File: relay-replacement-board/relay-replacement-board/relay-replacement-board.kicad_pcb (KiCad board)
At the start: 2 copper layers, 100 x 55 mm, 26 parts, among them J1 Conn_01x02, J10 Conn_01x02, J11 Conn_01x02, J12 Conn_01x02, J2 Conn_01x02, J3 Conn_01x02, J4 Conn_01x02, J5 Conn_01x02, J6 Conn_01x02, J7 Conn_01x02, J8 Conn_01x02, J9 Conn_01x02, Q1 NVD5865NL, Q2 NVD5865NL, Q3 NVD5865NL, Q4 NVD5865NL, Q5 NVD5865NL, Q6 NVD5865NL, Q7 NVD5865NL

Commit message: Trace routing
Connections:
- J4 pad 1: +12V -> Net-(J4-Pad1)
- J4 pad 2: Net-(J4-Pad2) -> +12V
- Q1 pad 2: Net-(J4-Pad2) -> Net-(J4-Pad1)
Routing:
- net /trigger1: track 0.00 -> 33.5 mm
- net /trigger5: track 0.00 -> 31.1 mm
- net /trigger3: track 0.00 -> 28.7 mm
- net /trigger2: track 0.00 -> 25.4 mm
- net /trigger6: track 0.00 -> 25.1 mm
- net /trigger4: track 0.00 -> 24.9 mm
- net /trigger0: track 0.00 -> 18.4 mm
- net Net-(J12-Pad2): track 0.00 -> 13.5 mm
- net Net-(J8-Pad2): track 0.00 -> 12.0 mm
- net Net-(J7-Pad2): track 0.00 -> 12.0 mm
- net Net-(J6-Pad2): track 0.00 -> 12.0 mm
- net Net-(J5-Pad2): track 0.00 -> 12.0 mm
- net Net-(J11-Pad2): track 0.00 -> 12.0 mm
- net Net-(J4-Pad1): track 0.00 -> 11.5 mm
- added copper zone on B.Cu, net +12V
- added copper zone on F.Cu, net GND
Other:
- net class Default: clearance 0.2 -> 0.75; trace_width 0.25 -> 0.5
- rule trace_clearance: 0.2 -> 0.75

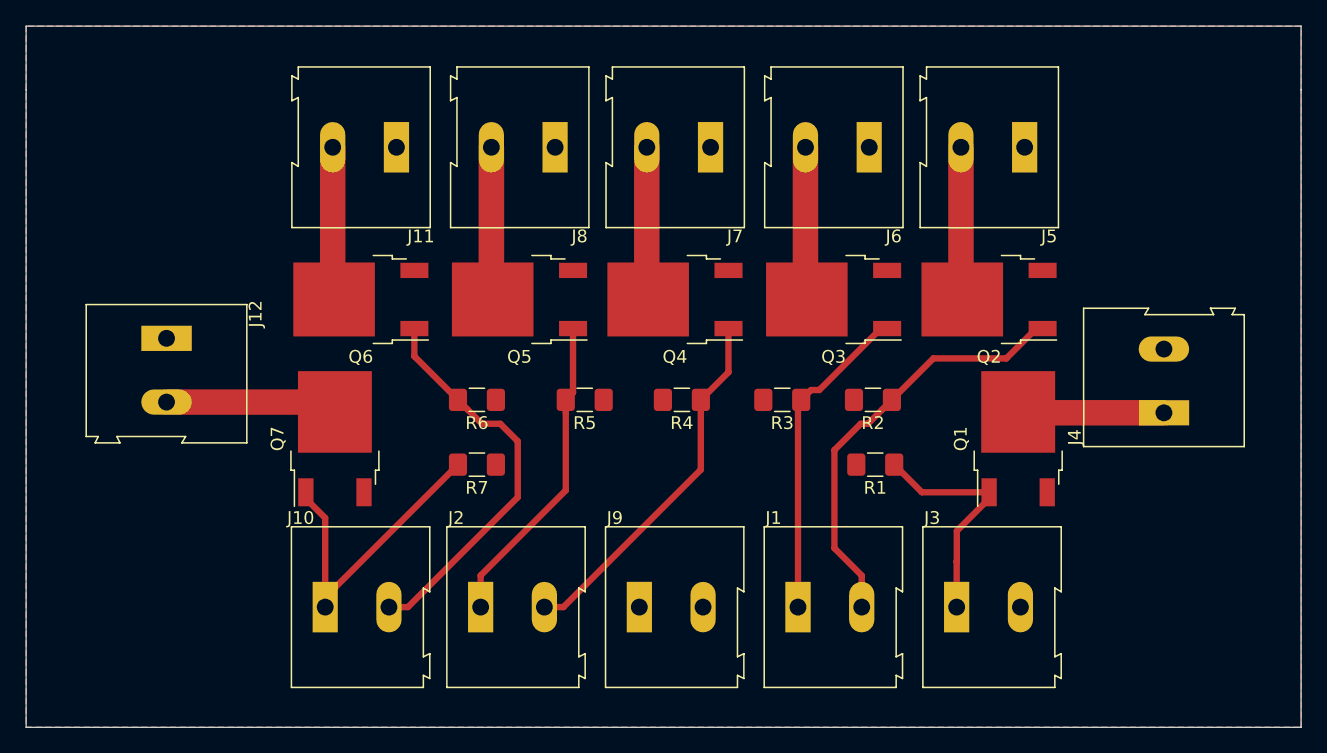
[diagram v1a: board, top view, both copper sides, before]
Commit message: M4 mounting holes
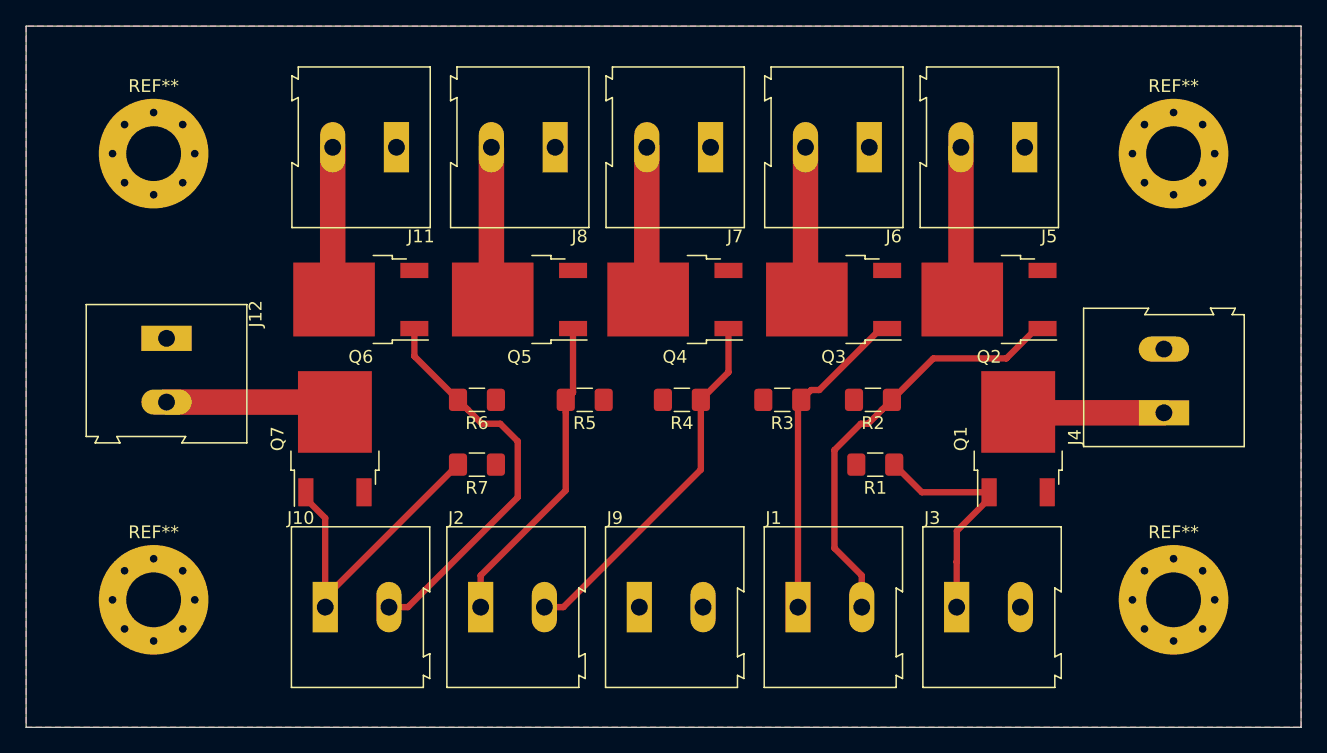
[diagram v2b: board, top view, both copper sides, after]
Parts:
- added REF**: MountingHole_4.3mm_M4_Pad_Via, MountingHole:MountingHole_4.3mm_M4_Pad_Via, F.Cu at (95.0, 80.0)
- added REF**: MountingHole_4.3mm_M4_Pad_Via, MountingHole:MountingHole_4.3mm_M4_Pad_Via, F.Cu at (95.0, 115.0)
- added REF**: MountingHole_4.3mm_M4_Pad_Via, MountingHole:MountingHole_4.3mm_M4_Pad_Via, F.Cu at (175.0, 115.0)
- added REF**: MountingHole_4.3mm_M4_Pad_Via, MountingHole:MountingHole_4.3mm_M4_Pad_Via, F.Cu at (175.0, 80.0)
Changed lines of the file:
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@@
     (tracks 63)
     (zones 0)
-    (modules 26)
+    (modules 30)
     (nets 17)
   )
@@
     (add_net "Net-(J8-Pad2)")
   )
+  (module MountingHole:MountingHole_4.3mm_M4_Pad_Via (layer F.Cu)
+    (at 95 80)
+    (descr "Mounting Hole 4.3mm, M4")
+    (tags "mounting hole 4.3mm m4")
+    (attr virtual)
+    (fp_text reference REF** (at 0 -5.3) (layer F.SilkS)
+      (effects (font (size 1 1) (thickness 0.15)))
+    )
+    (fp_text value MountingHole_4.3mm_M4_Pad_Via (at 0 5.3) (layer F.Fab)
+      (effects (font (size 1 1) (thickness 0.15)))
+    )
+    (fp_circle (center 0 0) (end 4.55 0) (layer F.CrtYd) (width 0.05))
+    (fp_circle (center 0 0) (end 4.3 0) (layer Cmts.User) (width 0.15))
+    (fp_text user %R (at 0.3 0) (layer F.Fab)
+      (effects (font (size 1 1) (thickness 0.15)))
+    )
+    (pad 1 thru_hole circle (at 2.280419 -2.280419) (size 0.9 0.9) (drill 0.6) (layers *.Cu *.Mask))
+    (pad 1 thru_hole circle (at 0 -3.225) (size 0.9 0.9) (drill 0.6) (layers *.Cu *.Mask))
+    (pad 1 thru_hole circle (at -2.280419 -2.280419) (size 0.9 0.9) (drill 0.6) (layers *.Cu *.Mask))
+    (pad 1 thru_hole circle (at -3.225 0) (size 0.9 0.9) (drill 0.6) (layers *.Cu *.Mask))
+    (pad 1 thru_hole circle (at -2.280419 2.280419) (size 0.9 0.9) (drill 0.6) (layers *.Cu *.Mask))
+    (pad 1 thru_hole circle (at 0 3.225) (size 0.9 0.9) (drill 0.6) (layers *.Cu *.Mask))
+    (pad 1 thru_hole circle (at 2.280419 2.280419) (size 0.9 0.9) (drill 0.6) (layers *.Cu *.Mask))
+    (pad 1 thru_hole circle (at 3.225 0) (size 0.9 0.9) (drill 0.6) (layers *.Cu *.Mask))
+    (pad 1 thru_hole circle (at 0 0) (size 8.6 8.6) (drill 4.3) (layers *.Cu *.Mask))
+  )
+  (module MountingHole:MountingHole_4.3mm_M4_Pad_Via (layer F.Cu)
+    (at 95 115)
+    (descr "Mounting Hole 4.3mm, M4")
+    (tags "mounting hole 4.3mm m4")
+    (attr virtual)
+    (fp_text reference REF** (at 0 -5.3) (layer F.SilkS)
+      (effects (font (size 1 1) (thickness 0.15)))
+    )
+    (fp_text value MountingHole_4.3mm_M4_Pad_Via (at 0 5.3) (layer F.Fab)
+      (effects (font (size 1 1) (thickness 0.15)))
+    )
+    (fp_circle (center 0 0) (end 4.55 0) (layer F.CrtYd) (width 0.05))
+    (fp_circle (center 0 0) (end 4.3 0) (layer Cmts.User) (width 0.15))
+    (fp_text user %R (at 0.3 0) (layer F.Fab)
+      (effects (font (size 1 1) (thickness 0.15)))
+    )
+    (pad 1 thru_hole circle (at 2.280419 -2.280419) (size 0.9 0.9) (drill 0.6) (layers *.Cu *.Mask))
+    (pad 1 thru_hole circle (at 0 -3.225) (size 0.9 0.9) (drill 0.6) (layers *.Cu *.Mask))
+    (pad 1 thru_hole circle (at -2.280419 -2.280419) (size 0.9 0.9) (drill 0.6) (layers *.Cu *.Mask))
+    (pad 1 thru_hole circle (at -3.225 0) (size 0.9 0.9) (drill 0.6) (layers *.Cu *.Mask))
+    (pad 1 thru_hole circle (at -2.280419 2.280419) (size 0.9 0.9) (drill 0.6) (layers *.Cu *.Mask))
+    (pad 1 thru_hole circle (at 0 3.225) (size 0.9 0.9) (drill 0.6) (layers *.Cu *.Mask))
+    (pad 1 thru_hole circle (at 2.280419 2.280419) (size 0.9 0.9) (drill 0.6) (layers *.Cu *.Mask))
+    (pad 1 thru_hole circle (at 3.225 0) (size 0.9 0.9) (drill 0.6) (layers *.Cu *.Mask))
+    (pad 1 thru_hole circle (at 0 0) (size 8.6 8.6) (drill 4.3) (layers *.Cu *.Mask))
+  )
+  (module MountingHole:MountingHole_4.3mm_M4_Pad_Via (layer F.Cu)
+    (at 175 115)
+    (descr "Mounting Hole 4.3mm, M4")
+    (tags "mounting hole 4.3mm m4")
+    (attr virtual)
+    (fp_text reference REF** (at 0 -5.3) (layer F.SilkS)
+      (effects (font (size 1 1) (thickness 0.15)))
+    )
+    (fp_text value MountingHole_4.3mm_M4_Pad_Via (at 0 5.3) (layer F.Fab)
+      (effects (font (size 1 1) (thickness 0.15)))
+    )
+    (fp_circle (center 0 0) (end 4.55 0) (layer F.CrtYd) (width 0.05))
+    (fp_circle (center 0 0) (end 4.3 0) (layer Cmts.User) (width 0.15))
+    (fp_text user %R (at 0.3 0) (layer F.Fab)
+      (effects (font (size 1 1) (thickness 0.15)))
+    )
+    (pad 1 thru_hole circle (at 2.280419 -2.280419) (size 0.9 0.9) (drill 0.6) (layers *.Cu *.Mask))
+    (pad 1 thru_hole circle (at 0 -3.225) (size 0.9 0.9) (drill 0.6) (layers *.Cu *.Mask))
+    (pad 1 thru_hole circle (at -2.280419 -2.280419) (size 0.9 0.9) (drill 0.6) (layers *.Cu *.Mask))
+    (pad 1 thru_hole circle (at -3.225 0) (size 0.9 0.9) (drill 0.6) (layers *.Cu *.Mask))
+    (pad 1 thru_hole circle (at -2.280419 2.280419) (size 0.9 0.9) (drill 0.6) (layers *.Cu *.Mask))
+    (pad 1 thru_hole circle (at 0 3.225) (size 0.9 0.9) (drill 0.6) (layers *.Cu *.Mask))
+    (pad 1 thru_hole circle (at 2.280419 2.280419) (size 0.9 0.9) (drill 0.6) (layers *.Cu *.Mask))
+    (pad 1 thru_hole circle (at 3.225 0) (size 0.9 0.9) (drill 0.6) (layers *.Cu *.Mask))
+    (pad 1 thru_hole circle (at 0 0) (size 8.6 8.6) (drill 4.3) (layers *.Cu *.Mask))
+  )
+  (module MountingHole:MountingHole_4.3mm_M4_Pad_Via (layer F.Cu)
+    (at 175 80)
+    (descr "Mounting Hole 4.3mm, M4")
+    (tags "mounting hole 4.3mm m4")
+    (attr virtual)
+    (fp_text reference REF** (at 0 -5.3) (layer F.SilkS)
+      (effects (font (size 1 1) (thickness 0.15)))
+    )
+    (fp_text value MountingHole_4.3mm_M4_Pad_Via (at 0 5.3) (layer F.Fab)
+      (effects (font (size 1 1) (thickness 0.15)))
+    )
+    (fp_circle (center 0 0) (end 4.55 0) (layer F.CrtYd) (width 0.05))
+    (fp_circle (center 0 0) (end 4.3 0) (layer Cmts.User) (width 0.15))
+    (fp_text user %R (at 0.3 0) (layer F.Fab)
+      (effects (font (size 1 1) (thickness 0.15)))
+    )
+    (pad 1 thru_hole circle (at 2.280419 -2.280419) (size 0.9 0.9) (drill 0.6) (layers *.Cu *.Mask))
+    (pad 1 thru_hole circle (at 0 -3.225) (size 0.9 0.9) (drill 0.6) (layers *.Cu *.Mask))
+    (pad 1 thru_hole circle (at -2.280419 -2.280419) (size 0.9 0.9) (drill 0.6) (layers *.Cu *.Mask))
+    (pad 1 thru_hole circle (at -3.225 0) (size 0.9 0.9) (drill 0.6) (layers *.Cu *.Mask))
+    (pad 1 thru_hole circle (at -2.280419 2.280419) (size 0.9 0.9) (drill 0.6) (layers *.Cu *.Mask))
+    (pad 1 thru_hole circle (at 0 3.225) (size 0.9 0.9) (drill 0.6) (layers *.Cu *.Mask))
+    (pad 1 thru_hole circle (at 2.280419 2.280419) (size 0.9 0.9) (drill 0.6) (layers *.Cu *.Mask))
+    (pad 1 thru_hole circle (at 3.225 0) (size 0.9 0.9) (drill 0.6) (layers *.Cu *.Mask))
+    (pad 1 thru_hole circle (at 0 0) (size 8.6 8.6) (drill 4.3) (layers *.Cu *.Mask))
+  )
   (module Resistor_SMD:R_1206_3216Metric_Pad1.42x1.75mm_HandSolder (layer F.Cu)

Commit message: added extra +12V in
The rated current on the terminal blocks is 16A each which is less than the possible current draw if every valve were on at the same time. This change increases the current capacity to and from the +12V rail to 32A.
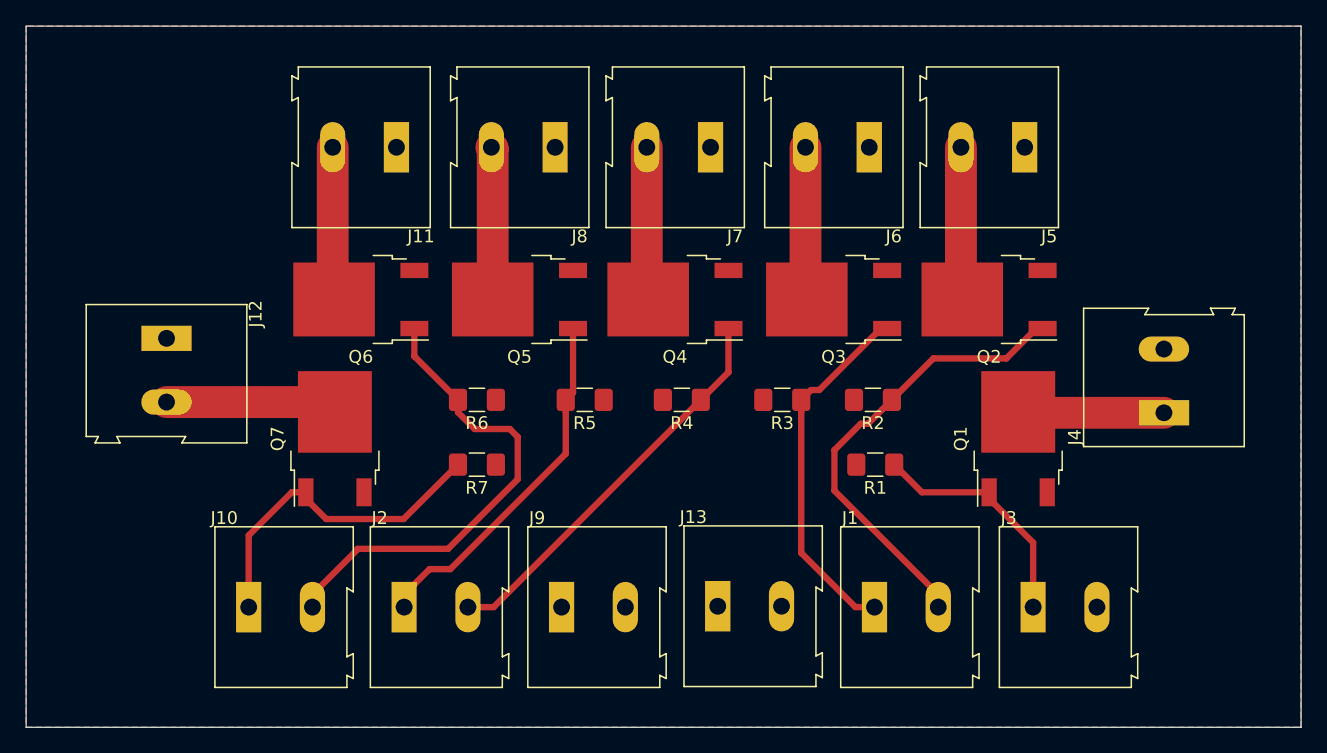
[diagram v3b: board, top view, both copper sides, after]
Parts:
- removed REF** (x4): MountingHole_4.3mm_M4_Pad_Via, MountingHole:MountingHole_4.3mm_M4_Pad_Via
- added J13: Conn_01x02, TerminalBlock:TerminalBlock_Altech_AK300-2_P5.00mm, F.Cu at (139.2, 115.5)
- moved J9 6.10 mm to (127.0, 115.6)
- moved J1 6.00 mm to (151.5, 115.6)
- moved J10 6.00 mm to (102.5, 115.6)
- moved J2 6.00 mm to (114.7, 115.6)
- moved J3 6.00 mm to (164.0, 115.6)
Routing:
- net /trigger5: track 31.1 -> 37.6 mm
- net /trigger4: track 24.9 -> 28.3 mm
- net /trigger2: track 25.4 -> 28.6 mm
- net /trigger3: track 28.7 -> 31.5 mm
- net /trigger1: track 33.5 -> 36.0 mm
- net /trigger6: track 25.1 -> 26.4 mm
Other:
- board text added: "7xMOSFET relay replacement board University of Southampton SUSF Lunar Hopper Harry Snell 2019"

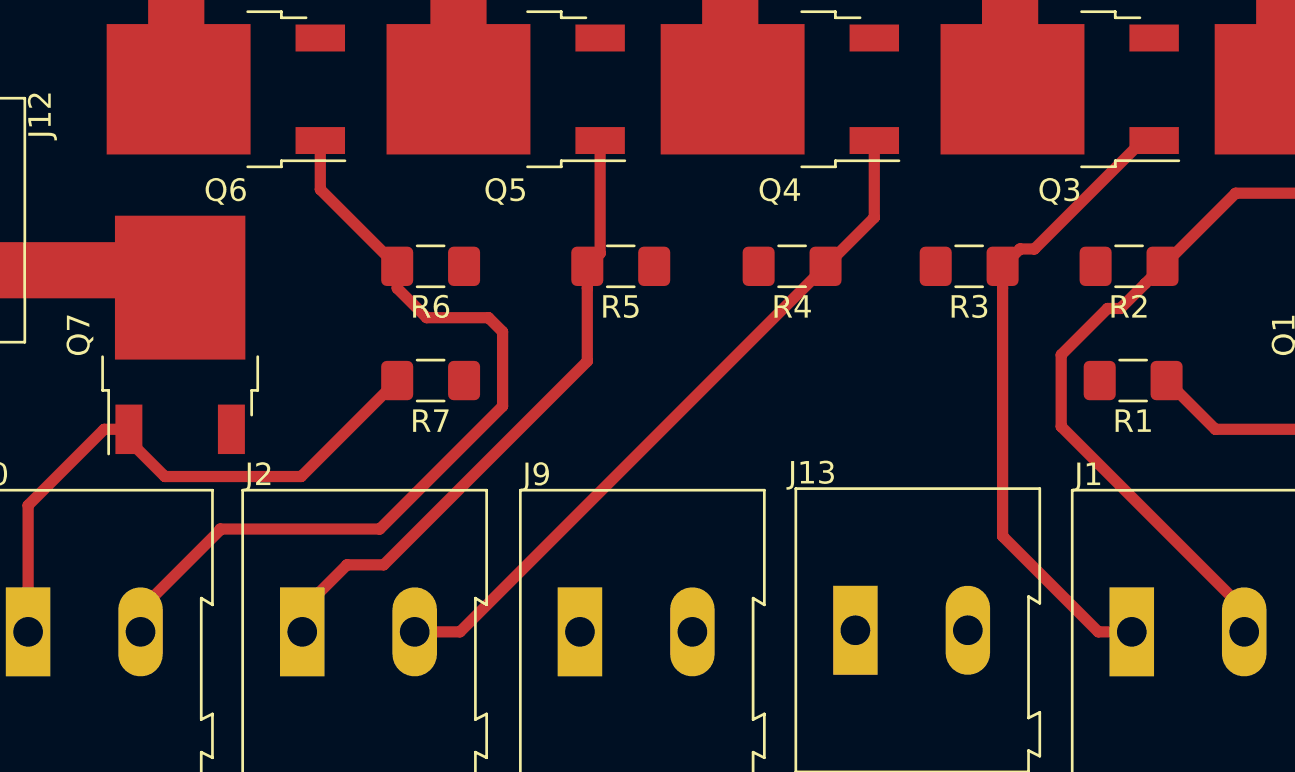
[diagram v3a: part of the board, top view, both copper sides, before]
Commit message: Minor adjustments to trace routing
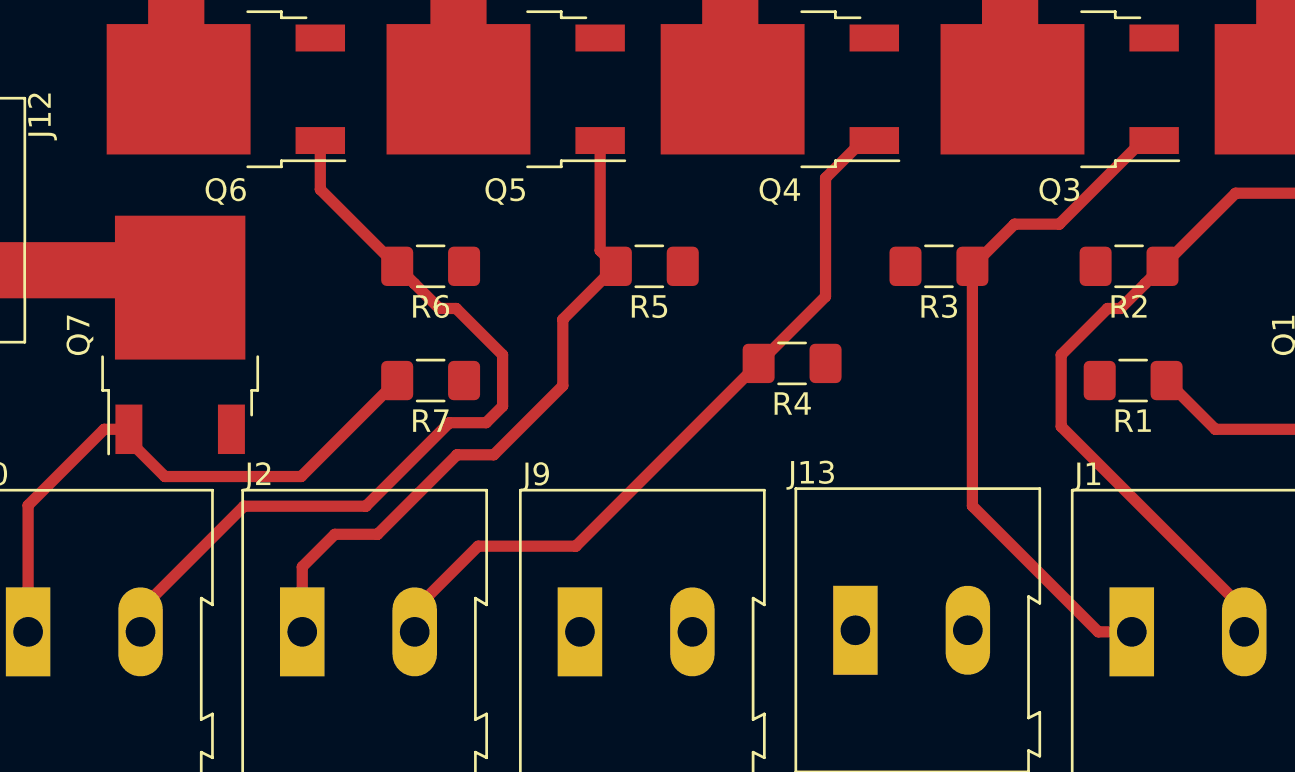
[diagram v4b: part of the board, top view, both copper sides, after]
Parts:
- moved R4 4.32 mm to (136.4, 103.6)
- moved R3 1.34 mm to (143.0, 99.3)
- moved R5 1.27 mm to (130.1, 99.3)
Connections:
- R4 pad 1: /trigger3 -> GND
- R4 pad 2: GND -> /trigger3
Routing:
- net /trigger4: track 28.3 -> 31.0 mm
- net /trigger2: track 28.6 -> 30.5 mm
- net /trigger3: track 31.5 -> 33.2 mm
- net /trigger5: track 37.6 -> 36.5 mm
